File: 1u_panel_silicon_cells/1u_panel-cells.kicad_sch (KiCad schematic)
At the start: 33 parts, among them U13 LTC4411, U14 LTC4411, U15 LTC4411, U16 LTC4411, U5 LTC4411, U6 LTC4411, U8 LTC4411, U9 LTC4411

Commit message: changes for silicon solar module bringup tasks
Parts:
- D12, D13: value KXOB2502X8F -> KXOB2502X8TF; footprint oresat-misc:KXOB2502X8F -> oresat-misc:KXOB2502X8TF; symbol oresat-misc:IXOLAR-KXOB2502X8F -> oresat-misc:IXOLAR-KXOB2502X8TF; DPN KXOB25-02X8FTR-ND -> KXOB25-02X8TF-TR
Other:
- note added: "2x IXOLAR KXOB2502X8TF 1.84cm^2 ea, Silicon - Voc = 5.53 V - Vmp = 4.46 V - Isc = 6.3/12.6 mA ea./tot. - Imp = 5.9/11.8 mA ea./tot. - Wmp = 26.3/52.6 mW ea./tot."
- note removed: "2x IXOLAR KXOB2502X8F 1.84cm^2 ea, Silicon - Voc = 5.53 V - Vmp = 4.46 V - Isc = 6.3/12.6 mA ea./tot. - Imp = 5.9/11.8 mA ea./tot. - Wmp = 26.3/52.6 mW ea./tot."
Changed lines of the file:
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@@
 		)
 	)
-	(text "2x IXOLAR KXOB2502X8F\n1.84cm^2 ea, Silicon\n- Voc = 5.53 V\n- Vmp = 4.46 V\n- Isc = 6.3/12.6 mA ea./tot.\n- Imp = 5.9/11.8 mA ea./tot.\n- Wmp = 26.3/52.6 mW ea./tot."
+	(text "2x IXOLAR KXOB2502X8TF\n1.84cm^2 ea, Silicon\n- Voc = 5.53 V\n- Vmp = 4.46 V\n- Isc = 6.3/12.6 mA ea./tot.\n- Imp = 5.9/11.8 mA ea./tot.\n- Wmp = 26.3/52.6 mW ea./tot."
 		(exclude_from_sim no)
 		(at 71.374 171.45 0)
@@
 	)
 	(symbol
-		(lib_id "oresat-misc:IXOLAR-KXOB2502X8F")
+		(lib_id "oresat-misc:IXOLAR-KXOB2502X8TF")
 		(at 124.46 203.2 0)
 		(unit 1)
@@
 			)
 		)
-		(property "Value" "KXOB2502X8F"
+		(property "Value" "KXOB2502X8TF"
 			(at 126.746 210.82 0)
 			(effects
@@
 			)
 		)
-		(property "Footprint" "oresat-misc:KXOB2502X8F"
+		(property "Footprint" "oresat-misc:KXOB2502X8TF"
 			(at 124.46 203.2 0)
 			(effects
@@
 			)
 		)
-		(property "Datasheet" "https://waf-e.dubudisk.com/anysolar.dubuplus.com/techsupport@anysolar.biz/O18Ae06/DubuDisk/www/Gen3/KXOB25-02X8F%20DATA%20SHEET%20202007.pdf"
+		(property "Datasheet" "https://waf-e.dubudisk.com/anysolar.dubuplus.com/techsupport@anysolar.biz/O18Atf8/DubuDisk/www/Gen3/KXOB25-02X8TF%20DATA%20SHEET%20202012.pdf"
 			(at 124.46 203.2 0)
 			(effects
@@
 			)
 		)
-		(property "Description" "Monocrystalline Solar Cell 26.3 mW 5.53 V"
+		(property "Description" "Monocrystalline Silicon Solar Cell 26.3 mW 5.53 V thin"
 			(at 124.46 203.2 0)
 			(effects
@@
 			)
 		)
-		(property "DPN" "KXOB25-02X8FTR-ND"
+		(property "DPN" "KXOB25-02X8TF-TR"
 			(at 124.46 203.2 0)
 			(effects
@@
 	)
 	(symbol
-		(lib_id "oresat-misc:IXOLAR-KXOB2502X8F")
+		(lib_id "oresat-misc:IXOLAR-KXOB2502X8TF")
 		(at 80.01 203.2 0)
 		(unit 1)
@@
 			)
 		)
-		(property "Value" "KXOB2502X8F"
+		(property "Value" "KXOB2502X8TF"
 			(at 82.296 210.82 0)
 			(effects
@@
 			)
 		)
-		(property "Footprint" "oresat-misc:KXOB2502X8F"
+		(property "Footprint" "oresat-misc:KXOB2502X8TF"
 			(at 80.01 203.2 0)
 			(effects
@@
 			)
 		)
-		(property "Datasheet" "https://waf-e.dubudisk.com/anysolar.dubuplus.com/techsupport@anysolar.biz/O18Ae06/DubuDisk/www/Gen3/KXOB25-02X8F%20DATA%20SHEET%20202007.pdf"
+		(property "Datasheet" "https://waf-e.dubudisk.com/anysolar.dubuplus.com/techsupport@anysolar.biz/O18Atf8/DubuDisk/www/Gen3/KXOB25-02X8TF%20DATA%20SHEET%20202012.pdf"
 			(at 80.01 203.2 0)
 			(effects
@@
 			)
 		)
-		(property "Description" "Monocrystalline Solar Cell 26.3 mW 5.53 V"
+		(property "Description" "Monocrystalline Silicon Solar Cell 26.3 mW 5.53 V thin"
 			(at 80.01 203.2 0)
 			(effects
@@
 			)
 		)
-		(property "DPN" "KXOB25-02X8FTR-ND"
+		(property "DPN" "KXOB25-02X8TF-TR"
 			(at 80.01 203.2 0)
 			(effects

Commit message: chages for https://github.com/oresat/oresat-solar-hardware/issues/53
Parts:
- added C38: 1u, oresat-passives:0603-C-NOSILK, symbol Device:C
- added C39, C40, C41, C42, C43, C44, C45: 4.7u, oresat-passives:0603-C-NOSILK, symbol Device:C
- C10: value 1u -> 4.7u; DPN 587-3473-1-ND -> 1276-1784-1-ND; MFR Taiyo Yuden -> Samsung Electro-Mechanics; MPN TMK107BJ105KAHT -> CL10A475KO8NNNC
- D12, D13: MPN KXOB25-02X8F-TR -> KXOB25-02X8TF-TR
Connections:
- net GND: now also C38.2, C39.2, C40.2, C41.2, C42.2, C43.2, C44.2, C45.2
- net VSOLAR: now also C10.1, C39.1, C40.1, C41.1, C42.1, C43.1, C44.1, C45.1
- net at D2.POS1 (A1), R5.1, U5.1: now also C38.1; no longer C10.1
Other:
- moved on the sheet: D10, D11, D12, D13, D2, D7, D8, D9, R28, R29, R30, R31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

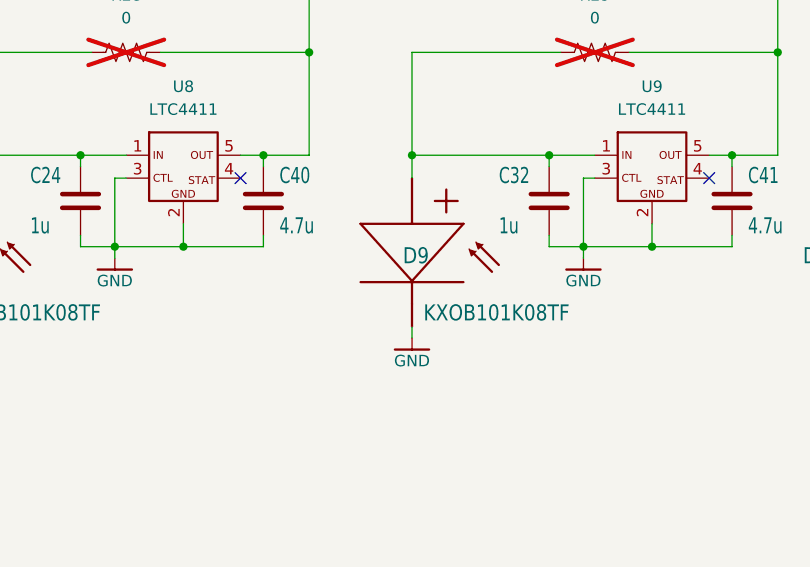
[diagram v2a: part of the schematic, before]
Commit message: changes for bringup issues on Si Solar module
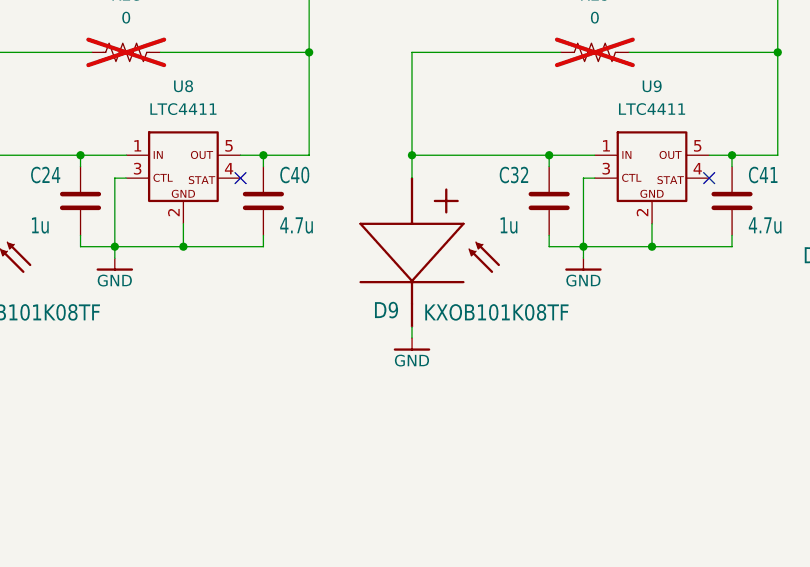
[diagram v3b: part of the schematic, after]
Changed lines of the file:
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@@
 (kicad_sch
-	(version 20231120)
+	(version 20250114)
 	(generator "eeschema")
-	(generator_version "8.0")
+	(generator_version "9.0")
 	(paper "USLedger")
 	(title_block
@@
 		(rev "1.0")
 	)
+	(rectangle
+		(start 44.45 35.56)
+		(end 392.43 227.33)
+		(stroke
+			(width 0)
+			(type default)
+		)
+		(fill
+			(type none)
+		)
+	)
+	(text "Combined IXOLAR KXOB series cells, Silicon\n- Voc = 5.53 V\n- Vmp = 4.46 V\n- Isc = 269.4 mA\n- Imp = 253 mA\n- Wmp = 1128.4 mW"
+		(exclude_from_sim no)
+		(at 156.718 70.612 0)
+		(effects
+			(font
+				(size 1.778 1.27)
+			)
+			(justify left bottom)
+		)
+	)
+	(text "2x IXOLAR KXOB2502X8TF\n1.84cm^2 ea, Silicon\n- Voc = 5.53 V\n- Vmp = 4.46 V\n- Isc = 6.3/12.6 mA ea./tot.\n- Imp = 5.9/11.8 mA ea./tot.\n- Wmp = 26.3/52.6 mW ea./tot."
+		(exclude_from_sim no)
+		(at 63.754 168.91 0)
+		(effects
+			(font
+				(size 1.778 1.27)
+			)
+			(justify left bottom)
+		)
+	)
+	(text "Solar Cells"
+		(exclude_from_sim no)
+		(at 155.956 45.466 0)
+		(effects
+			(font
+				(size 3.81 3.2385)
+			)
+			(justify left bottom)
+		)
+	)
+	(text "6x IXOLAR KXOB101K08TF\n9.66cm^2 ea, Silicon\n- Voc = 5.53 V\n- Vmp = 4.46 V\n- Isc = 42.8/256.8 mA ea./tot.\n- Imp = 40.2/241.2 mA ea./tot.\n- Wmp = 179.292/1075 mw ea./tot."
+		(exclude_from_sim no)
+		(at 64.008 90.17 0)
+		(effects
+			(font
+				(size 1.778 1.27)
+			)
+			(justify left bottom)
+		)
+	)
 	(junction
 		(at 191.77 127)
@@
 		)
 	)
-	(rectangle
-		(start 44.45 35.56)
-		(end 392.43 227.33)
-		(stroke
-			(width 0)
-			(type default)
-		)
-		(fill
-			(type none)
-		)
-	)
-	(text "Combined IXOLAR KXOB series cells, Silicon\n- Voc = 5.53 V\n- Vmp = 4.46 V\n- Isc = 269.4 mA\n- Imp = 253 mA\n- Wmp = 1128.4 mW"
-		(exclude_from_sim no)
-		(at 156.718 70.612 0)
-		(effects
-			(font
-				(size 1.778 1.27)
-			)
-			(justify left bottom)
-		)
-	)
-	(text "2x IXOLAR KXOB2502X8TF\n1.84cm^2 ea, Silicon\n- Voc = 5.53 V\n- Vmp = 4.46 V\n- Isc = 6.3/12.6 mA ea./tot.\n- Imp = 5.9/11.8 mA ea./tot.\n- Wmp = 26.3/52.6 mW ea./tot."
-		(exclude_from_sim no)
-		(at 63.754 168.91 0)
-		(effects
-			(font
-				(size 1.778 1.27)
-			)
-			(justify left bottom)
-		)
-	)
-	(text "Solar Cells"
-		(exclude_from_sim no)
-		(at 155.956 45.466 0)
-		(effects
-			(font
-				(size 3.81 3.2385)
-			)
-			(justify left bottom)
-		)
-	)
-	(text "6x IXOLAR KXOB101K08TF\n9.66cm^2 ea, Silicon\n- Voc = 5.53 V\n- Vmp = 4.46 V\n- Isc = 42.8/256.8 mA ea./tot.\n- Imp = 40.2/241.2 mA ea./tot.\n- Wmp = 179.292/1075 mw ea./tot."
-		(exclude_from_sim no)
-		(at 64.008 90.17 0)
-		(effects
-			(font
-				(size 1.778 1.27)
-			)
-			(justify left bottom)
-		)
-	)
 	(symbol
 		(lib_id "oresat-diodes:LTC4411")
@@
 		(dnp no)
 		(property "Reference" "D9"
-			(at 223.774 128.016 0)
+			(at 220.472 134.112 0)
 			(effects
 				(font
@@
 		(at 254 87.63 0)
 		(unit 1)
-		(exclude_from_sim yes)
+		(exclude_from_sim no)
 		(in_bom no)
 		(on_board yes)

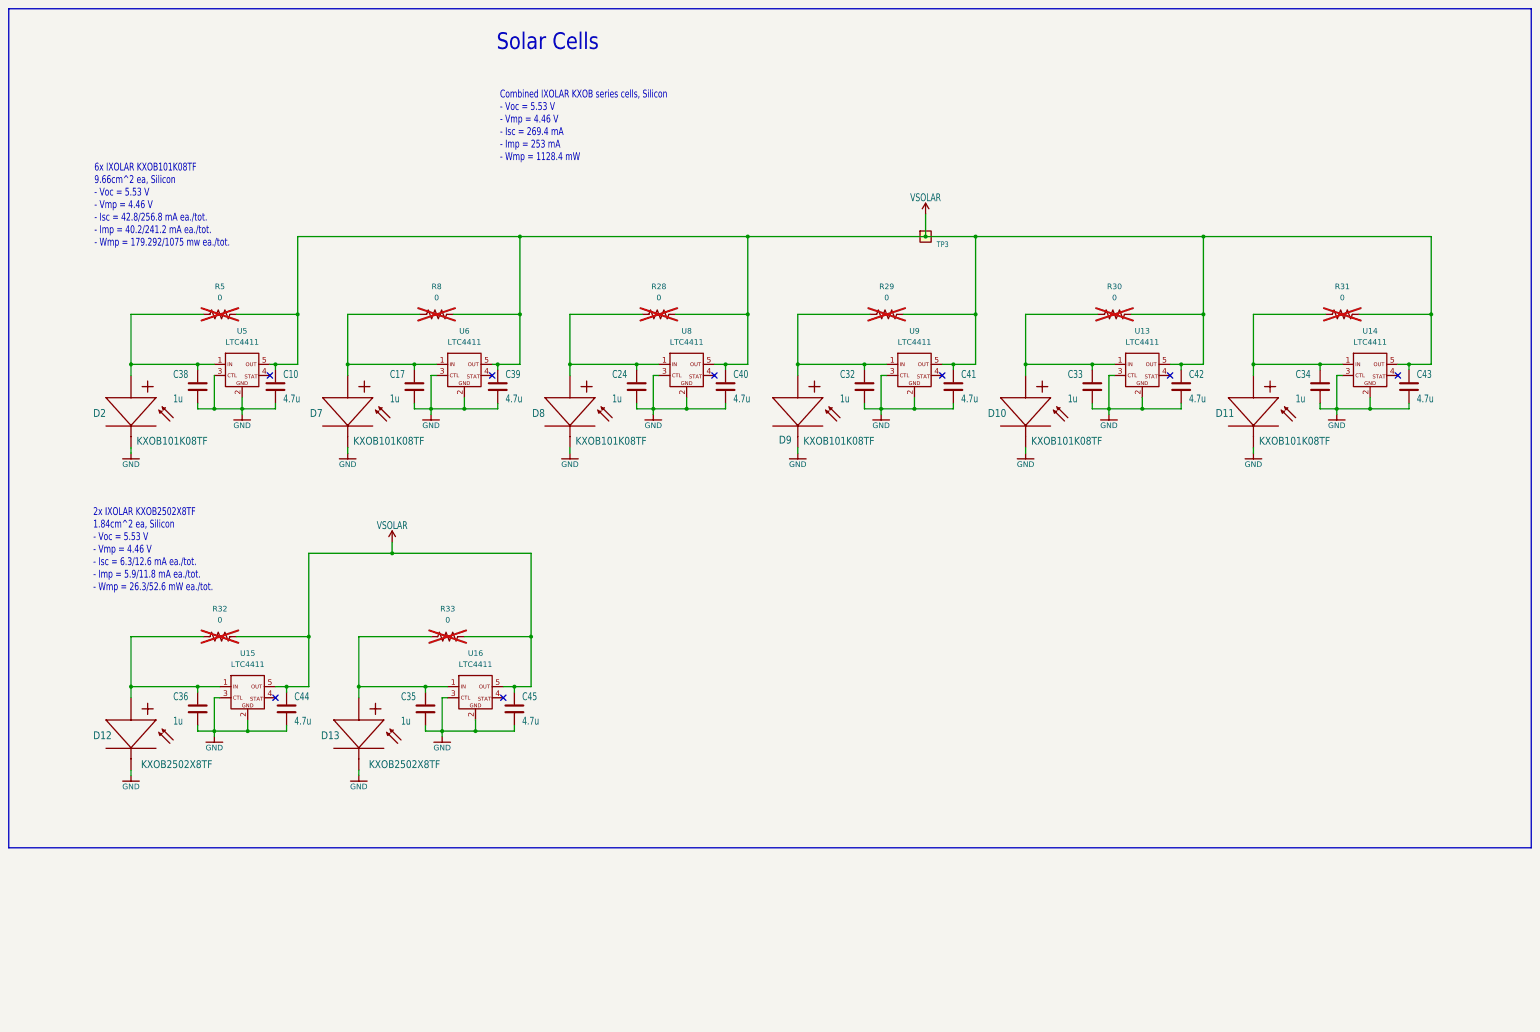
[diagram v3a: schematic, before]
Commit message: Cleanup before fab! Added pullup resistors to ALERTs on TMP101s, removed some paranoia hardware including test points and pullups we don't need, did some schematic polishing for prettiness, and cleaned up some of the zones onthe layout. Removed the need for any old import or local symbol or footprint libraries. Upgraded to v1.1.
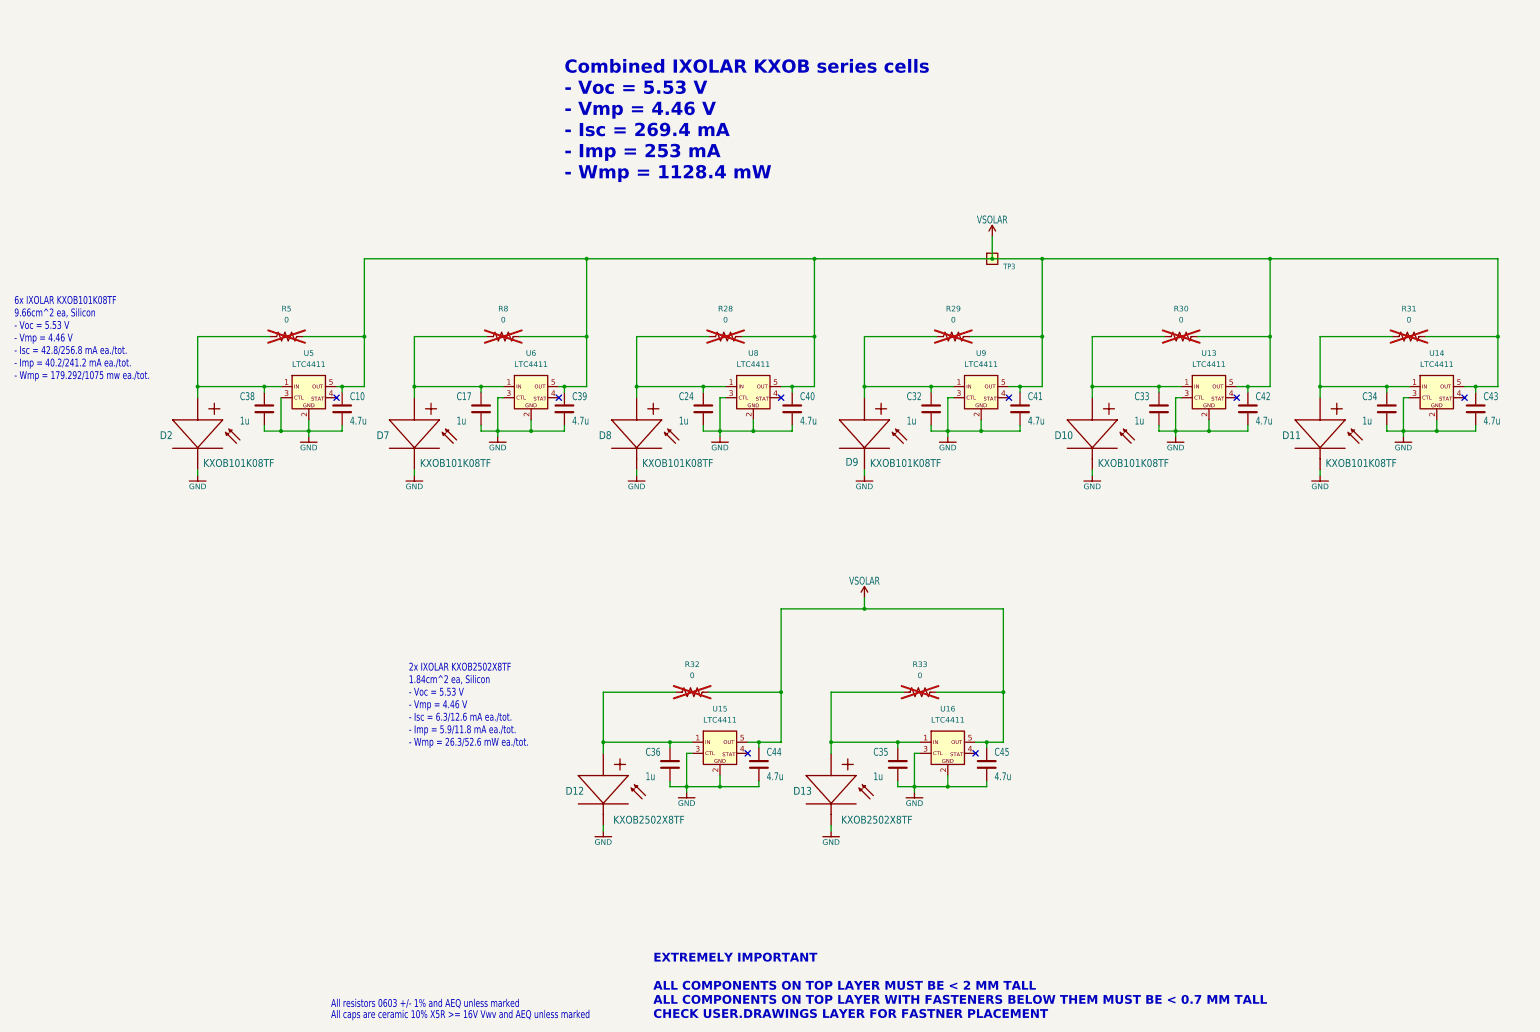
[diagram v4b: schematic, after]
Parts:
- C10, C17, C24, C32, C33, C34, C35, C36, C38, C39, C40, C41, C42, C43, C44, C45, D10, D11, D12, D13, D2, D7, D8, D9, R28, R29, R30, R31, R32, R33, R5, R8, U13, U14, U15, U16, U5, U6, U8, U9: Distributor Digi-Key -> (none)
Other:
- note added: "All caps are ceramic 10% X5R >= 16V Vwv and AEQ unless marked"
- note added: "All resistors 0603 +/- 1% and AEQ unless marked"
- note added: "Combined IXOLAR KXOB series cells - Voc = 5.53 V - Vmp = 4.46 V - Isc = 269.4 mA - Imp = 253 mA - Wmp = 1128.4 mW"
- note added: "EXTREMELY IMPORTANT ALL COMPONENTS ON TOP LAYER MUST BE < 2 MM TALL ALL COMPONENTS ON TOP LAYER WITH FASTENERS BELOW THEM MUST BE < 0.7 MM TALL CHECK USER.DRAWINGS LAYER FOR FASTNER PLACEMENT"
- note removed: "Combined IXOLAR KXOB series cells, Silicon - Voc = 5.53 V - Vmp = 4.46 V - Isc = 269.4 mA - Imp = 253 mA - Wmp = 1128.4 mW"
- note removed: "Solar Cells"
- moved on the sheet: C10, C17, C24, C32, C33, C34, C35, C36, C38, C39, C40, C41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
